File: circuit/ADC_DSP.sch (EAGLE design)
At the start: 76 parts, among them IC1 REG1117, IC3 STM32F40XRXT6, IC4 CS4272, Q1 8MHz, Q2 24.576MHz

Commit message: - плата, которую будем травить
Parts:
- R28, R29: value 1.2k -> 120
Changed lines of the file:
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@@
 <part name="GND21" library="supply1" deviceset="GND" device=""/>
 <part name="USB" library="con-phoenix-254" deviceset="MPT3" device=""/>
-<part name="R28" library="rcl" deviceset="R-EU_" device="R0603" value="1.2k"/>
-<part name="R29" library="rcl" deviceset="R-EU_" device="R0603" value="1.2k"/>
+<part name="R28" library="rcl" deviceset="R-EU_" device="R0603" value="120"/>
+<part name="R29" library="rcl" deviceset="R-EU_" device="R0603" value="120"/>
 <part name="R32" library="rcl" deviceset="R-EU_" device="R0603" value="10k"/>
 <part name="R34" library="rcl" deviceset="R-EU_" device="R0603" value="10k"/>

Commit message: - работающий DDS
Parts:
- C25, C35: value 2.2u -> 1u
- C27, C28: value 1.5n -> 4.7n
- R28, R29: value 120 -> 150
- R32, R34: value 10k -> 12k
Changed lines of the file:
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@@
 <part name="P+5" library="supply1" deviceset="+5V" device=""/>
 <part name="GND19" library="supply1" deviceset="GND" device=""/>
-<part name="C27" library="rcl" deviceset="C-EU" device="C0805" value="1.5n"/>
-<part name="C28" library="rcl" deviceset="C-EU" device="C0805" value="1.5n"/>
+<part name="C27" library="rcl" deviceset="C-EU" device="C0805" value="4.7n"/>
+<part name="C28" library="rcl" deviceset="C-EU" device="C0805" value="4.7n"/>
 <part name="C5" library="rcl" deviceset="CPOL-EU" device="153CLV-0605" value="220uF"/>
 <part name="R1" library="rcl" deviceset="R-EU_" device="R0603" value="220"/>
@@
 <part name="GND21" library="supply1" deviceset="GND" device=""/>
 <part name="USB" library="con-phoenix-254" deviceset="MPT3" device=""/>
-<part name="R28" library="rcl" deviceset="R-EU_" device="R0603" value="120"/>
-<part name="R29" library="rcl" deviceset="R-EU_" device="R0603" value="120"/>
-<part name="R32" library="rcl" deviceset="R-EU_" device="R0603" value="10k"/>
-<part name="R34" library="rcl" deviceset="R-EU_" device="R0603" value="10k"/>
-<part name="C25" library="rcl" deviceset="C-EU" device="C0603" value="2.2u"/>
-<part name="C35" library="rcl" deviceset="C-EU" device="C0603" value="2.2u"/>
+<part name="R28" library="rcl" deviceset="R-EU_" device="R0603" value="150"/>
+<part name="R29" library="rcl" deviceset="R-EU_" device="R0603" value="150"/>
+<part name="R32" library="rcl" deviceset="R-EU_" device="R0603" value="12k"/>
+<part name="R34" library="rcl" deviceset="R-EU_" device="R0603" value="12k"/>
+<part name="C25" library="rcl" deviceset="C-EU" device="C0603" value="1u"/>
+<part name="C35" library="rcl" deviceset="C-EU" device="C0603" value="1u"/>
 <part name="U$1" library="balmer" deviceset="SN74LVC1G3157DBVR" device=""/>
 <part name="U$2" library="balmer" deviceset="SN74LVC1G3157DBVR" device=""/>

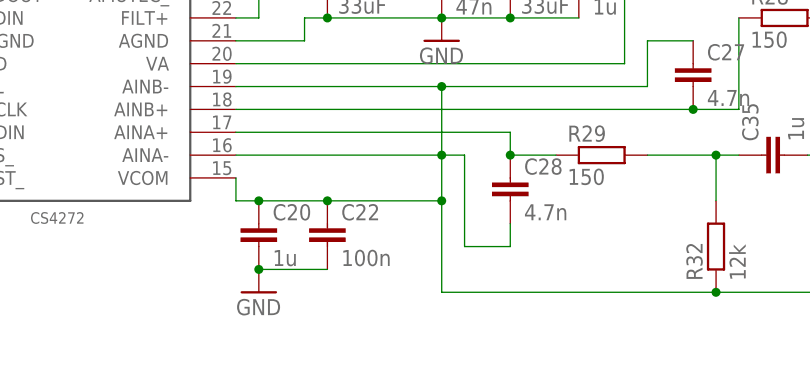
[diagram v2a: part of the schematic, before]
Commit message: - была ошибка в TimeMs() - конденсатор 100 uF на VCOM - не успевает выводить на дисплей и обрабатывать звук.
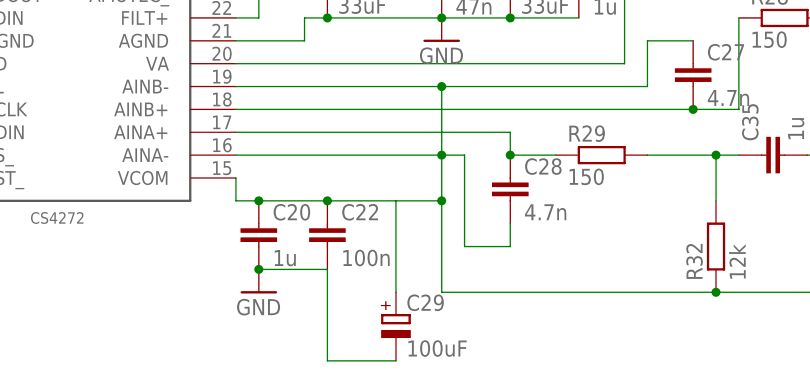
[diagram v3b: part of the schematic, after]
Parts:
- added C29: 100uF, rcl:CPOL-EU153CLV-0605
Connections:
- net GND: now also C29.-
- net VCOM: now also C29.+
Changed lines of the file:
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@@
 <grid distance="0.1" unitdist="inch" unit="inch" style="lines" multiple="1" display="no" altdistance="0.01" altunitdist="inch" altunit="inch"/>
 <layers>
-<layer number="1" name="Top" color="4" fill="1" visible="no" active="no"/>
-<layer number="16" name="Bottom" color="1" fill="1" visible="no" active="no"/>
-<layer number="17" name="Pads" color="2" fill="1" visible="no" active="no"/>
-<layer number="18" name="Vias" color="2" fill="1" visible="no" active="no"/>
-<layer number="19" name="Unrouted" color="6" fill="1" visible="no" active="no"/>
-<layer number="20" name="Dimension" color="15" fill="1" visible="no" active="no"/>
-<layer number="21" name="tPlace" color="7" fill="1" visible="no" active="no"/>
-<layer number="22" name="bPlace" color="7" fill="1" visible="no" active="no"/>
-<layer number="23" name="tOrigins" color="15" fill="1" visible="no" active="no"/>
-<layer number="24" name="bOrigins" color="15" fill="1" visible="no" active="no"/>
-<layer number="25" name="tNames" color="7" fill="1" visible="no" active="no"/>
-<layer number="26" name="bNames" color="7" fill="1" visible="no" active="no"/>
-<layer number="27" name="tValues" color="7" fill="1" visible="no" active="no"/>
-<layer number="28" name="bValues" color="7" fill="1" visible="no" active="no"/>
+<layer number="1" name="Top" color="4" fill="1" visible="yes" active="no"/>
+<layer number="16" name="Bottom" color="1" fill="1" visible="yes" active="no"/>
+<layer number="17" name="Pads" color="2" fill="1" visible="yes" active="no"/>
+<layer number="18" name="Vias" color="2" fill="1" visible="yes" active="no"/>
+<layer number="19" name="Unrouted" color="6" fill="1" visible="yes" active="no"/>
+<layer number="20" name="Dimension" color="15" fill="1" visible="yes" active="no"/>
+<layer number="21" name="tPlace" color="7" fill="1" visible="yes" active="no"/>
+<layer number="22" name="bPlace" color="7" fill="1" visible="yes" active="no"/>
+<layer number="23" name="tOrigins" color="15" fill="1" visible="yes" active="no"/>
+<layer number="24" name="bOrigins" color="15" fill="1" visible="yes" active="no"/>
+<layer number="25" name="tNames" color="7" fill="1" visible="yes" active="no"/>
+<layer number="26" name="bNames" color="7" fill="1" visible="yes" active="no"/>
+<layer number="27" name="tValues" color="7" fill="1" visible="yes" active="no"/>
+<layer number="28" name="bValues" color="7" fill="1" visible="yes" active="no"/>
 <layer number="29" name="tStop" color="7" fill="3" visible="no" active="no"/>
 <layer number="30" name="bStop" color="7" fill="6" visible="no" active="no"/>
@@
 <layer number="35" name="tGlue" color="7" fill="4" visible="no" active="no"/>
 <layer number="36" name="bGlue" color="7" fill="5" visible="no" active="no"/>
-<layer number="37" name="tTest" color="7" fill="1" visible="no" active="no"/>
-<layer number="38" name="bTest" color="7" fill="1" visible="no" active="no"/>
+<layer number="37" name="tTest" color="7" fill="1" visible="yes" active="no"/>
+<layer number="38" name="bTest" color="7" fill="1" visible="yes" active="no"/>
 <layer number="39" name="tKeepout" color="4" fill="11" visible="no" active="no"/>
 <layer number="40" name="bKeepout" color="1" fill="11" visible="no" active="no"/>
@@
 <layer number="44" name="Drills" color="7" fill="1" visible="no" active="no"/>
 <layer number="45" name="Holes" color="7" fill="1" visible="no" active="no"/>
-<layer number="46" name="Milling" color="3" fill="1" visible="no" active="no"/>
-<layer number="47" name="Measures" color="7" fill="1" visible="no" active="no"/>
-<layer number="48" name="Document" color="7" fill="1" visible="no" active="no"/>
-<layer number="49" name="Reference" color="7" fill="1" visible="no" active="no"/>
-<layer number="50" name="dxf" color="7" fill="1" visible="no" active="no"/>
-<layer number="51" name="tDocu" color="7" fill="1" visible="no" active="no"/>
-<layer number="52" name="bDocu" color="7" fill="1" visible="no" active="no"/>
-<layer number="53" name="tGND_GNDA" color="7" fill="9" visible="no" active="no"/>
-<layer number="54" name="bGND_GNDA" color="1" fill="9" visible="no" active="no"/>
-<layer number="56" name="wert" color="7" fill="1" visible="no" active="no"/>
+<layer number="46" name="Milling" color="3" fill="1" visible="yes" active="no"/>
+<layer number="47" name="Measures" color="7" fill="1" visible="yes" active="no"/>
+<layer number="48" name="Document" color="7" fill="1" visible="yes" active="no"/>
+<layer number="49" name="Reference" color="7" fill="1" visible="yes" active="no"/>
+<layer number="50" name="dxf" color="7" fill="1" visible="yes" active="no"/>
+<layer number="51" name="tDocu" color="7" fill="1" visible="yes" active="no"/>
+<layer number="52" name="bDocu" color="7" fill="1" visible="yes" active="no"/>
+<layer number="53" name="tGND_GNDA" color="7" fill="9" visible="yes" active="no"/>
+<layer number="54" name="bGND_GNDA" color="1" fill="9" visible="yes" active="no"/>
+<layer number="56" name="wert" color="7" fill="1" visible="yes" active="no"/>
 <layer number="90" name="Modules" color="5" fill="1" visible="yes" active="yes"/>
 <layer number="91" name="Nets" color="2" fill="1" visible="yes" active="yes"/>
@@
 <part name="C13" library="rcl" deviceset="C-EU" device="C0603" value="100n"/>
 <part name="GND28" library="supply1" deviceset="GND" device=""/>
+<part name="C29" library="rcl" deviceset="CPOL-EU" device="153CLV-0605" value="100uF"/>
 </parts>
 <sheets>
@@
 <instance part="C13" gate="G$1" x="251.46" y="22.86"/>
 <instance part="GND28" gate="1" x="251.46" y="15.24"/>
+<instance part="C29" gate="G$1" x="195.58" y="-25.4"/>
 </instances>
 <busses>
@@
 <pinref part="GND19" gate="1" pin="GND"/>
 <junction x="180.34" y="-20.32"/>
+<pinref part="C29" gate="G$1" pin="-"/>
+<wire x1="195.58" y1="-30.48" x2="187.96" y2="-30.48" width="0.1524" layer="91"/>
+<wire x1="187.96" y1="-30.48" x2="187.96" y2="-20.32" width="0.1524" layer="91"/>
 </segment>
 <segment>
@@
 <wire x1="177.8" y1="-12.7" x2="177.8" y2="-10.16" width="0.1524" layer="91"/>
 <junction x="180.34" y="-12.7"/>
-<wire x1="187.96" y1="-12.7" x2="200.66" y2="-12.7" width="0.1524" layer="91"/>
+<wire x1="187.96" y1="-12.7" x2="195.58" y2="-12.7" width="0.1524" layer="91"/>
 <junction x="187.96" y="-12.7"/>
+<wire x1="195.58" y1="-12.7" x2="200.66" y2="-12.7" width="0.1524" layer="91"/>
 <wire x1="200.66" y1="-12.7" x2="200.66" y2="-22.86" width="0.1524" layer="91"/>
 <wire x1="200.66" y1="-22.86" x2="231.14" y2="-22.86" width="0.1524" layer="91"/>
@@
 <junction x="200.66" y="-7.62"/>
 <junction x="200.66" y="-12.7"/>
-</segment>
-</net>
+<pinref part="C29" gate="G$1" pin="+"/>
+<wire x1="195.58" y1="-22.86" x2="195.58" y2="-12.7" width="0.1524" layer="91"/>
+</segment>
+</net>

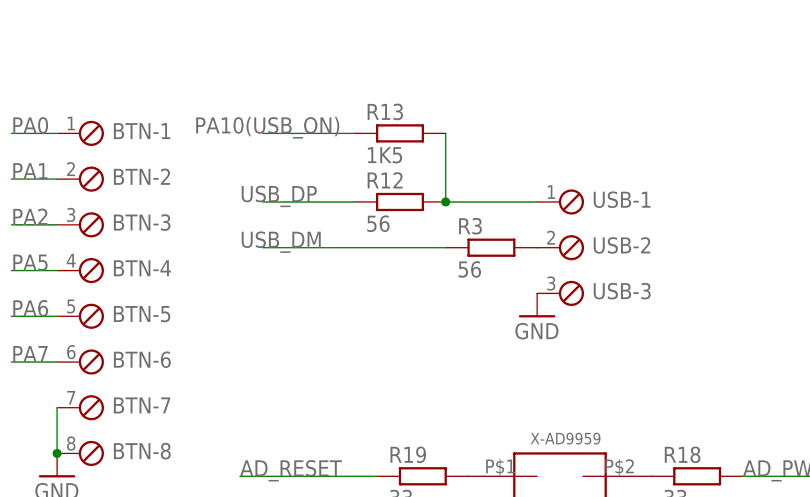
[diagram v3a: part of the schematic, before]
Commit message: - работающий в первом приближении USB Virtual Com Port
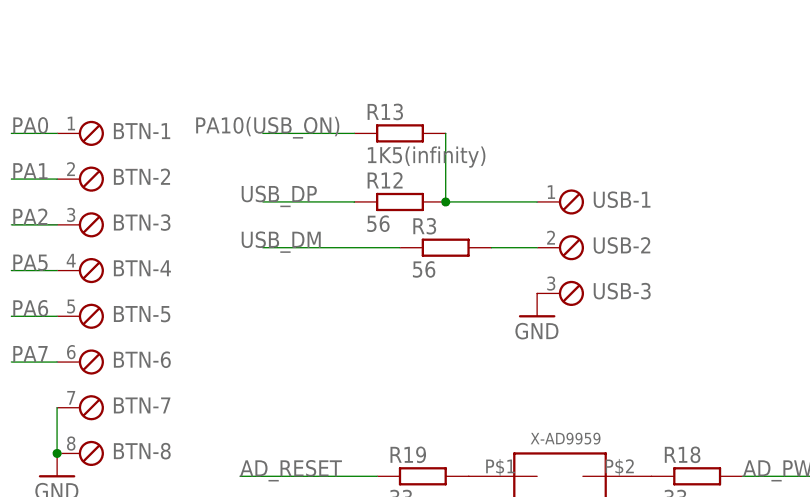
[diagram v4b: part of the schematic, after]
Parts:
- R13: value 1K5 -> 1K5(infinity)
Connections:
- net N$16 renamed D+
- net N$3 renamed D-
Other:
- moved on the sheet: R3
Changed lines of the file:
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@@
 <grid distance="0.1" unitdist="inch" unit="inch" style="lines" multiple="1" display="no" altdistance="0.01" altunitdist="inch" altunit="inch"/>
 <layers>
-<layer number="1" name="Top" color="4" fill="1" visible="yes" active="no"/>
-<layer number="16" name="Bottom" color="1" fill="1" visible="yes" active="no"/>
-<layer number="17" name="Pads" color="2" fill="1" visible="yes" active="no"/>
-<layer number="18" name="Vias" color="2" fill="1" visible="yes" active="no"/>
-<layer number="19" name="Unrouted" color="6" fill="1" visible="yes" active="no"/>
-<layer number="20" name="Dimension" color="15" fill="1" visible="yes" active="no"/>
-<layer number="21" name="tPlace" color="7" fill="1" visible="yes" active="no"/>
-<layer number="22" name="bPlace" color="7" fill="1" visible="yes" active="no"/>
-<layer number="23" name="tOrigins" color="15" fill="1" visible="yes" active="no"/>
-<layer number="24" name="bOrigins" color="15" fill="1" visible="yes" active="no"/>
-<layer number="25" name="tNames" color="7" fill="1" visible="yes" active="no"/>
-<layer number="26" name="bNames" color="7" fill="1" visible="yes" active="no"/>
-<layer number="27" name="tValues" color="7" fill="1" visible="yes" active="no"/>
-<layer number="28" name="bValues" color="7" fill="1" visible="yes" active="no"/>
+<layer number="1" name="Top" color="4" fill="1" visible="no" active="no"/>
+<layer number="16" name="Bottom" color="1" fill="1" visible="no" active="no"/>
+<layer number="17" name="Pads" color="2" fill="1" visible="no" active="no"/>
+<layer number="18" name="Vias" color="2" fill="1" visible="no" active="no"/>
+<layer number="19" name="Unrouted" color="6" fill="1" visible="no" active="no"/>
+<layer number="20" name="Dimension" color="15" fill="1" visible="no" active="no"/>
+<layer number="21" name="tPlace" color="7" fill="1" visible="no" active="no"/>
+<layer number="22" name="bPlace" color="7" fill="1" visible="no" active="no"/>
+<layer number="23" name="tOrigins" color="15" fill="1" visible="no" active="no"/>
+<layer number="24" name="bOrigins" color="15" fill="1" visible="no" active="no"/>
+<layer number="25" name="tNames" color="7" fill="1" visible="no" active="no"/>
+<layer number="26" name="bNames" color="7" fill="1" visible="no" active="no"/>
+<layer number="27" name="tValues" color="7" fill="1" visible="no" active="no"/>
+<layer number="28" name="bValues" color="7" fill="1" visible="no" active="no"/>
 <layer number="29" name="tStop" color="7" fill="3" visible="no" active="no"/>
 <layer number="30" name="bStop" color="7" fill="6" visible="no" active="no"/>
@@
 <layer number="35" name="tGlue" color="7" fill="4" visible="no" active="no"/>
 <layer number="36" name="bGlue" color="7" fill="5" visible="no" active="no"/>
-<layer number="37" name="tTest" color="7" fill="1" visible="yes" active="no"/>
-<layer number="38" name="bTest" color="7" fill="1" visible="yes" active="no"/>
+<layer number="37" name="tTest" color="7" fill="1" visible="no" active="no"/>
+<layer number="38" name="bTest" color="7" fill="1" visible="no" active="no"/>
 <layer number="39" name="tKeepout" color="4" fill="11" visible="no" active="no"/>
 <layer number="40" name="bKeepout" color="1" fill="11" visible="no" active="no"/>
@@
 <layer number="44" name="Drills" color="7" fill="1" visible="no" active="no"/>
 <layer number="45" name="Holes" color="7" fill="1" visible="no" active="no"/>
-<layer number="46" name="Milling" color="3" fill="1" visible="yes" active="no"/>
-<layer number="47" name="Measures" color="7" fill="1" visible="yes" active="no"/>
-<layer number="48" name="Document" color="7" fill="1" visible="yes" active="no"/>
-<layer number="49" name="Reference" color="7" fill="1" visible="yes" active="no"/>
-<layer number="50" name="dxf" color="7" fill="1" visible="yes" active="no"/>
-<layer number="51" name="tDocu" color="7" fill="1" visible="yes" active="no"/>
-<layer number="52" name="bDocu" color="7" fill="1" visible="yes" active="no"/>
-<layer number="53" name="tGND_GNDA" color="7" fill="9" visible="yes" active="no"/>
-<layer number="54" name="bGND_GNDA" color="1" fill="9" visible="yes" active="no"/>
-<layer number="56" name="wert" color="7" fill="1" visible="yes" active="no"/>
+<layer number="46" name="Milling" color="3" fill="1" visible="no" active="no"/>
+<layer number="47" name="Measures" color="7" fill="1" visible="no" active="no"/>
+<layer number="48" name="Document" color="7" fill="1" visible="no" active="no"/>
+<layer number="49" name="Reference" color="7" fill="1" visible="no" active="no"/>
+<layer number="50" name="dxf" color="7" fill="1" visible="no" active="no"/>
+<layer number="51" name="tDocu" color="7" fill="1" visible="no" active="no"/>
+<layer number="52" name="bDocu" color="7" fill="1" visible="no" active="no"/>
+<layer number="53" name="tGND_GNDA" color="7" fill="9" visible="no" active="no"/>
+<layer number="54" name="bGND_GNDA" color="1" fill="9" visible="no" active="no"/>
+<layer number="56" name="wert" color="7" fill="1" visible="no" active="no"/>
 <layer number="90" name="Modules" color="5" fill="1" visible="yes" active="yes"/>
 <layer number="91" name="Nets" color="2" fill="1" visible="yes" active="yes"/>
@@
 <part name="R3" library="rcl" deviceset="R-EU_" device="R0603" value="56"/>
 <part name="R12" library="rcl" deviceset="R-EU_" device="R0603" value="56"/>
-<part name="R13" library="rcl" deviceset="R-EU_" device="R0603" value="1K5"/>
+<part name="R13" library="rcl" deviceset="R-EU_" device="R0603" value="1K5(infinity)"/>
 <part name="R14" library="rcl" deviceset="R-EU_" device="R0603" value="33"/>
 <part name="R15" library="rcl" deviceset="R-EU_" device="R0603" value="33"/>
@@
 <instance part="+3V2" gate="G$1" x="185.42" y="71.12"/>
 <instance part="GND4" gate="1" x="165.1" y="106.68"/>
-<instance part="R3" gate="G$1" x="160.02" y="114.3"/>
+<instance part="R3" gate="G$1" x="154.94" y="114.3"/>
 <instance part="R12" gate="G$1" x="149.86" y="119.38"/>
 <instance part="R13" gate="G$1" x="149.86" y="127"/>
@@
 <segment>
 <pinref part="R3" gate="G$1" pin="1"/>
-<wire x1="154.94" y1="114.3" x2="134.62" y2="114.3" width="0.1524" layer="91"/>
+<wire x1="149.86" y1="114.3" x2="134.62" y2="114.3" width="0.1524" layer="91"/>
 <label x="132.08" y="114.3" size="1.778" layer="95"/>
 </segment>
@@
 </segment>
 </net>
-<net name="N$16" class="0">
+<net name="D+" class="0">
 <segment>
 <pinref part="R12" gate="G$1" pin="2"/>
@@
 </segment>
 </net>
-<net name="N$3" class="0">
+<net name="D-" class="0">
 <segment>
 <pinref part="R3" gate="G$1" pin="2"/>
 <pinref part="USB" gate="-2" pin="1"/>
-</segment>
-</net>
+<wire x1="160.02" y1="114.3" x2="165.1" y2="114.3" width="0.1524" layer="91"/>
+</segment>
+</net>
